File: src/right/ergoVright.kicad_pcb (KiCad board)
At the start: 2 copper layers, 133.4 x 86.2 mm, 63 parts, among them J1 USB_C_Receptacle_USB2.0_16P, Q1 AO3401A, SW1 SW_Push_3pin_GND, SW10 SW_Push_3pin_GND, SW11 SW_Push_3pin_GND, SW12 SW_Push_3pin_GND, SW13 SW_Push_3pin_GND, SW14 SW_Push_3pin_GND, SW15 SW_Push_3pin_GND, SW16 SW_Push_3pin_GND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

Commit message: Finished pcb, started working on readme
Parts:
- added H1: MountingHole, MountingHole:MountingHole_2.7mm_M2.5, F.Cu at (186.7, 116.7)
- added H2: MountingHole, MountingHole:MountingHole_2.7mm_M2.5, F.Cu at (201.0, 116.7)
- moved D1 2.50 mm to (251.2, 72.2)
- moved D13 2.50 mm to (251.2, 110.1)
- moved D14 2.50 mm to (232.1, 110.3)
- moved D2 2.50 mm to (232.2, 72.2)
- moved D7 2.50 mm to (251.2, 91.2)
- moved D8 2.50 mm to (232.1, 91.2)
- moved SW1 2.50 mm to (251.0, 74.5)
- moved SW13 2.50 mm to (251.0, 112.5)
- moved SW14 2.50 mm to (232.0, 112.5)
- moved SW2 2.50 mm to (232.0, 74.5)
- moved SW7 2.50 mm to (251.0, 93.5)
- moved SW8 2.50 mm to (232.0, 93.5)
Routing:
- net ROW2: track 145.9 -> 144.9 mm
- net COL0: track 171.1 -> 170.0 mm
- net ROW0: track 131.6 -> 130.6 mm
- net ROW1: track 122.5 -> 121.5 mm
- net COL1: track 135.1 -> 134.0 mm
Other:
- outline, holes or cut-outs redrawn

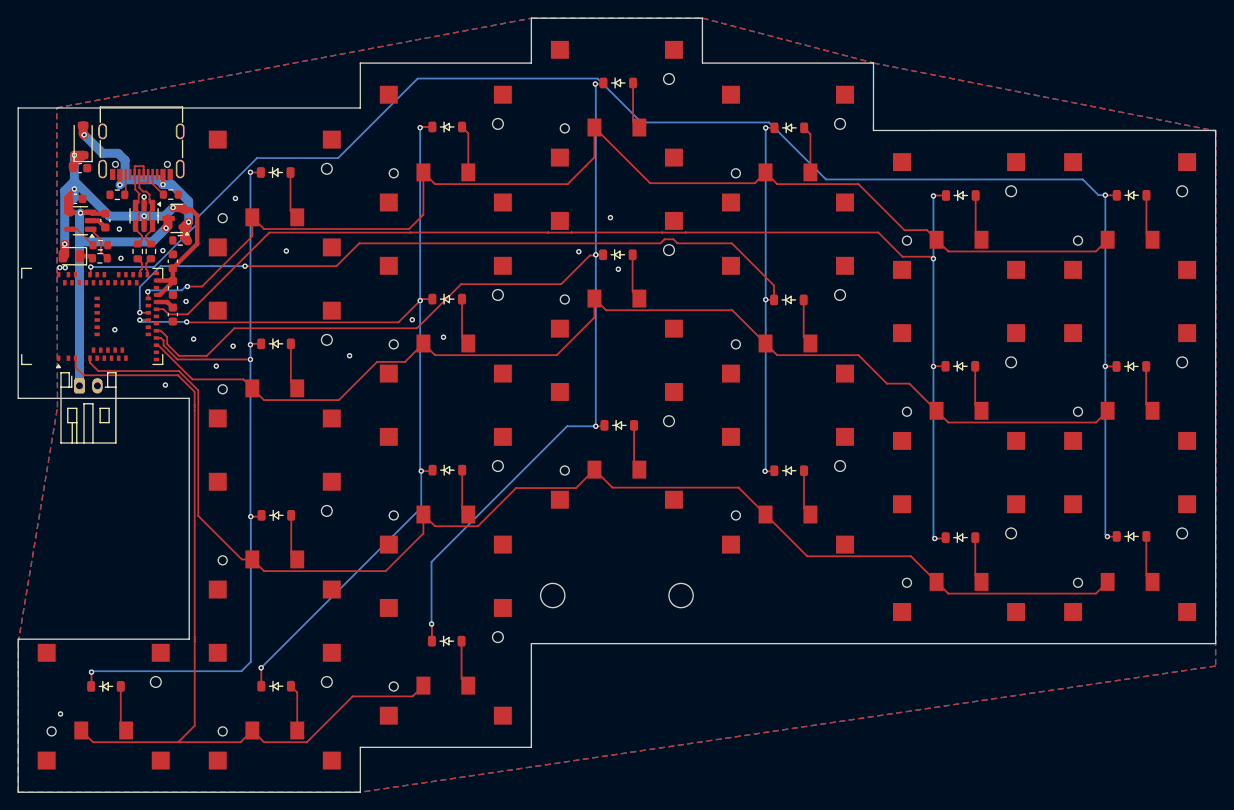
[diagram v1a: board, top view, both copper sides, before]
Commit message: Finished readme and updated the pcb
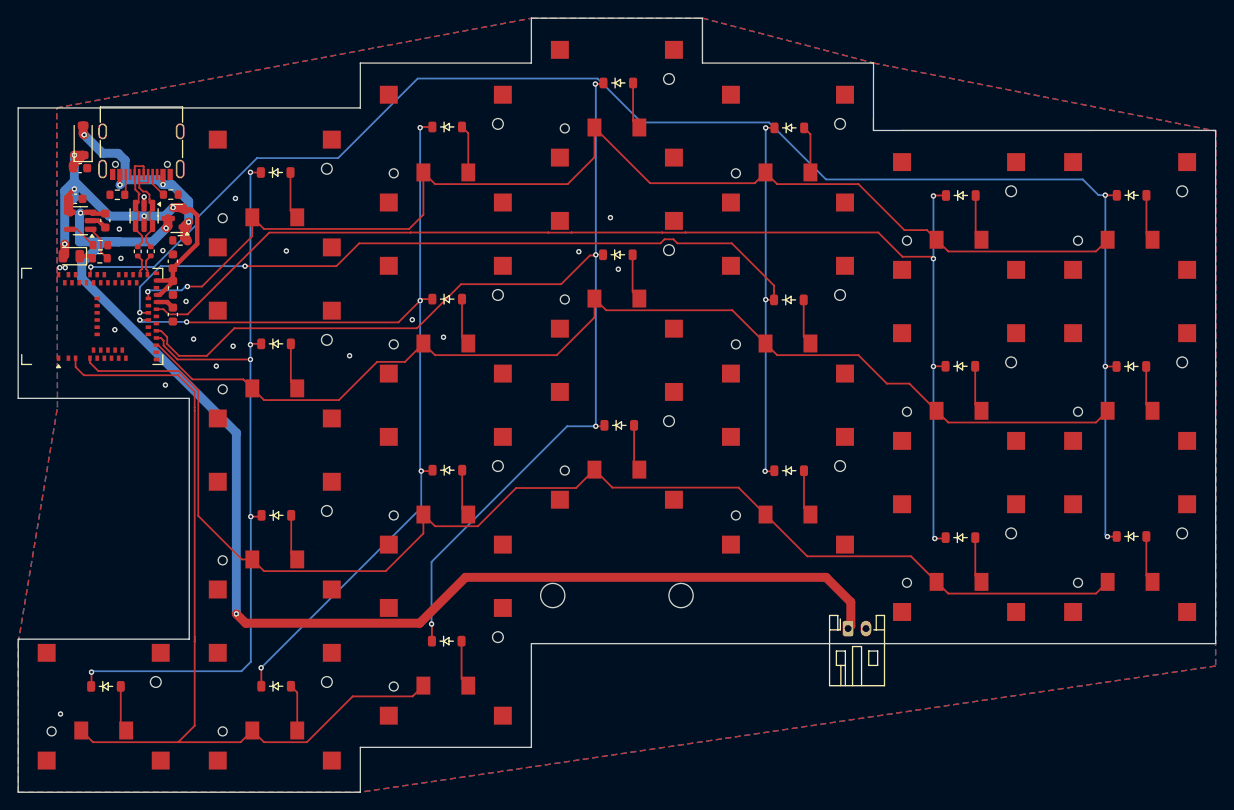
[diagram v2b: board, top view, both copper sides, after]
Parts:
- R1, R2: footprint Resistor_SMD:R_0603_1608Metric -> Resistor_SMD:R_0402_1005Metric
- moved BT1 89.8 mm to (219.6, 120.4)
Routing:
- net VBAT: track 33.6 -> 144.1 mm, vias 2 -> 3
